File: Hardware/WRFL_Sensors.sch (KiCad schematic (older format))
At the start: 15 parts, among them P10 TEST_POINT, P11 TEST_POINT, P12 JST_XH_8, P9 TEST_POINT, U5 TPS73633DBV, U6 MS5611-01BA03

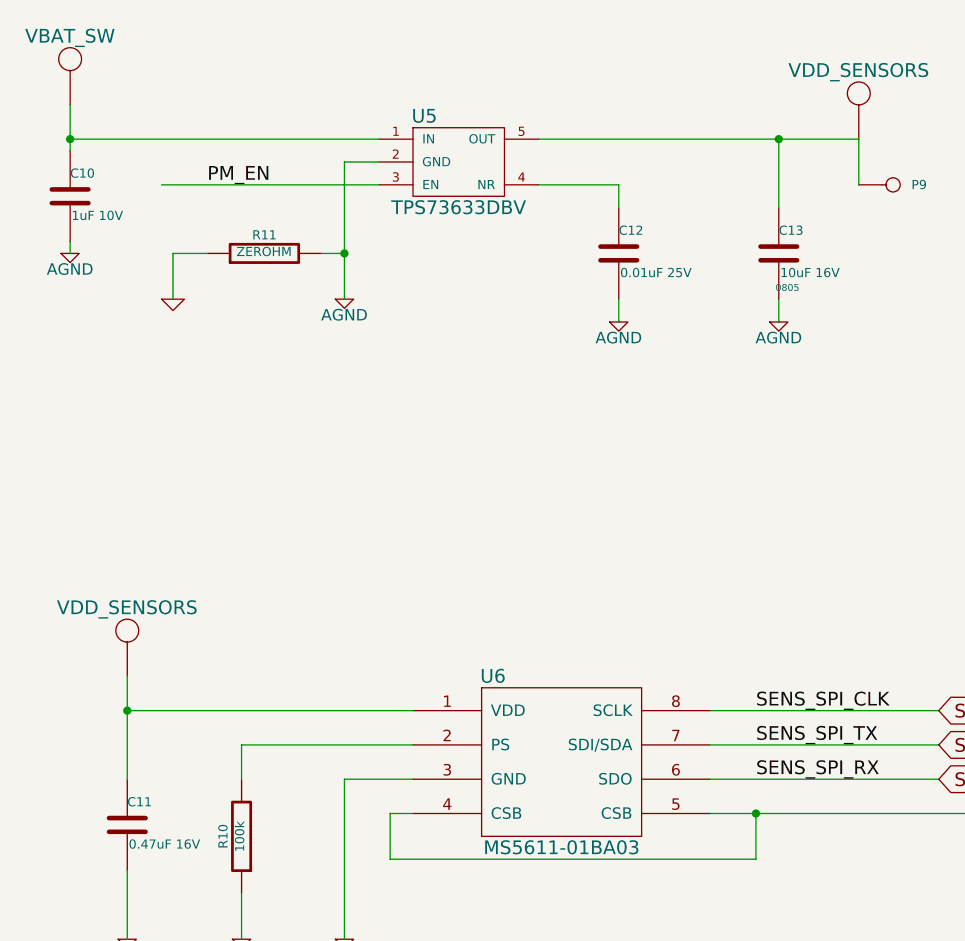
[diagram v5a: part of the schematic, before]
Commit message: MCU function assignment
BT RTS/CTS as test points,
BT reset GPIO option
Launchpad header pin function assignment (for ERC check)
Power symbols corrections
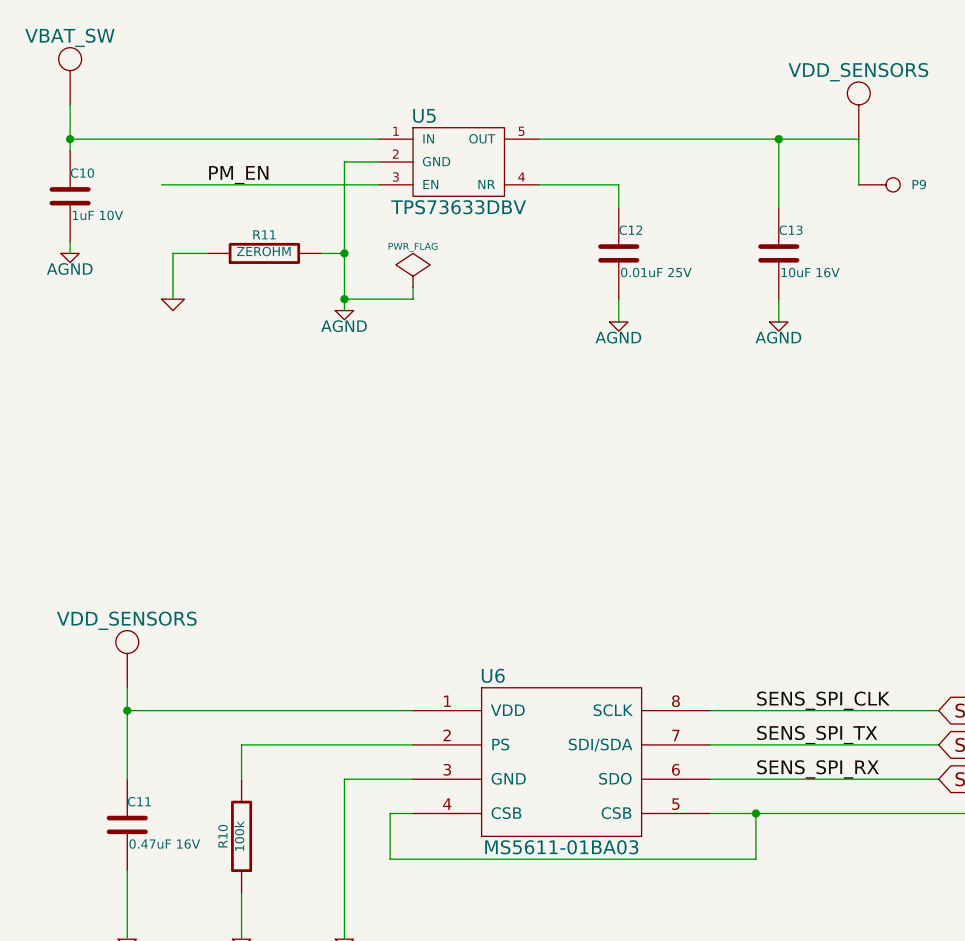
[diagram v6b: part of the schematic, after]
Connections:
- wire segments 50 -> 52
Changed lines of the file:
@@
-EESchema Schematic File Version 2  date Tuesday, October 15, 2013 09:37:22 AM
+EESchema Schematic File Version 2  date Tuesday, October 22, 2013 02:02:38 PM
 LIBS:power
 LIBS:device
@@
 Sheet 5 6
 Title ""
-Date "15 oct 2013"
+Date "22 oct 2013"
 Rev ""
 Comp "Nightmechanic"
@@
 Comment4 ""
 $EndDescr
-$Comp
-L VDD_SENSORS #U20
-U 1 1 524D591B
-P 4450 1800
-F 0 "#U20" H 4450 2000 60  0001 C CNN
-F 1 "VDD_SENSORS" H 4450 1900 60  0000 C CNN
-F 2 "" H 4450 1800 60  0000 C CNN
-F 3 "" H 4450 1800 60  0000 C CNN
-	1    4450 1800
-	1    0    0    -1
-$EndComp
 Wire Wire Line
 	1000 2450 1000 2500
@@
 $EndComp
 Wire Wire Line
-	2200 2100 2200 2700
+	2200 2100 2200 2750
 Wire Wire Line
 	2350 2100 2200 2100
@@
 	4100 2700 4100 2800
 $Comp
-L GND #PWR44
+L GND #PWR066
 U 1 1 524D593E
 P 1450 2700
-F 0 "#PWR44" H 1450 2700 30  0001 C CNN
+F 0 "#PWR066" H 1450 2700 30  0001 C CNN
 F 1 "GND" H 1450 2630 30  0001 C CNN
 F 2 "" H 1450 2700 60  0000 C CNN
@@
 $EndComp
 $Comp
-L AGND #PWR46
+L AGND #PWR067
 U 1 1 524D5944
-P 2200 2700
-F 0 "#PWR46" H 2200 2700 40  0001 C CNN
-F 1 "AGND" H 2200 2630 50  0000 C CNN
-F 2 "" H 2200 2700 60  0000 C CNN
-F 3 "" H 2200 2700 60  0000 C CNN
-	1    2200 2700
-	1    0    0    -1
-$EndComp
-$Comp
-L AGND #PWR49
+P 2200 2750
+F 0 "#PWR067" H 2200 2750 40  0001 C CNN
+F 1 "AGND" H 2200 2680 50  0000 C CNN
+F 2 "" H 2200 2750 60  0000 C CNN
+F 3 "" H 2200 2750 60  0000 C CNN
+	1    2200 2750
+	1    0    0    -1
+$EndComp
+$Comp
+L AGND #PWR068
 U 1 1 524D594A
 P 4100 2800
-F 0 "#PWR49" H 4100 2800 40  0001 C CNN
+F 0 "#PWR068" H 4100 2800 40  0001 C CNN
 F 1 "AGND" H 4100 2730 50  0000 C CNN
 F 2 "" H 4100 2800 60  0000 C CNN
@@
 $EndComp
 $Comp
-L AGND #PWR48
+L AGND #PWR069
 U 1 1 524D5950
 P 3400 2800
-F 0 "#PWR48" H 3400 2800 40  0001 C CNN
+F 0 "#PWR069" H 3400 2800 40  0001 C CNN
 F 1 "AGND" H 3400 2730 50  0000 C CNN
 F 2 "" H 3400 2800 60  0000 C CNN
@@
 F 0 "C13" H 4100 2600 40  0000 L CNN
 F 1 "10uF 16V" H 4106 2415 40  0000 L CNN
-F 2 "0805" H 4138 2350 30  0000 C CNN
+F 2 "0805" H 4138 2350 30  0001 C CNN
 F 3 "~" H 4100 2500 60  0000 C CNN
 	1    4100 2500
@@
 PM_EN
 $Comp
-L VBAT_SW #U18
+L VBAT_SW #U070
 U 1 1 5251CA9A
 P 1000 1650
-F 0 "#U18" H 1000 1850 60  0001 C CNN
+F 0 "#U070" H 1000 1850 60  0001 C CNN
 F 1 "VBAT_SW" H 1000 1750 60  0000 C CNN
 F 2 "~" H 1000 1650 60  0000 C CNN
@@
 $EndComp
 Connection ~ 1000 2000
-$Comp
-L VDD_SENSORS #U22
-U 1 1 5251CABC
-P 9350 900
-F 0 "#U22" H 9350 1100 60  0001 C CNN
-F 1 "VDD_SENSORS" H 9350 1000 60  0000 C CNN
-F 2 "~" H 9350 900 60  0000 C CNN
-F 3 "~" H 9350 900 60  0000 C CNN
-	1    9350 900
-	1    0    0    -1
-$EndComp
 $Comp
 L CONN_8 P12
@@
 $EndComp
 $Comp
-L AGND #PWR45
+L AGND #PWR071
 U 1 1 5251D2F7
 P 1750 5500
-F 0 "#PWR45" H 1750 5500 40  0001 C CNN
+F 0 "#PWR071" H 1750 5500 40  0001 C CNN
 F 1 "AGND" H 1750 5430 50  0000 C CNN
 F 2 "" H 1750 5500 60  0000 C CNN
@@
 $EndComp
 $Comp
-L VDD_SENSORS #U19
-U 1 1 5251D30C
-P 1250 4150
-F 0 "#U19" H 1250 4350 60  0001 C CNN
-F 1 "VDD_SENSORS" H 1250 4250 60  0000 C CNN
-F 2 "~" H 1250 4150 60  0000 C CNN
-F 3 "~" H 1250 4150 60  0000 C CNN
-	1    1250 4150
-	1    0    0    -1
-$EndComp
-$Comp
-L AGND #PWR47
+L AGND #PWR072
 U 1 1 5251D323
 P 2200 5500
-F 0 "#PWR47" H 2200 5500 40  0001 C CNN
+F 0 "#PWR072" H 2200 5500 40  0001 C CNN
 F 1 "AGND" H 2200 5430 50  0000 C CNN
 F 2 "" H 2200 5500 60  0000 C CNN
@@
 Wire Wire Line
 	2500 4500 1250 4500
-Wire Wire Line
-	1250 4350 1250 4800
 Wire Wire Line
 	1750 4650 1750 4800
@@
 Connection ~ 1250 4500
 $Comp
-L AGND #PWR43
+L AGND #PWR073
 U 1 1 5251D411
 P 1250 5500
-F 0 "#PWR43" H 1250 5500 40  0001 C CNN
+F 0 "#PWR073" H 1250 5500 40  0001 C CNN
 F 1 "AGND" H 1250 5430 50  0000 C CNN
 F 2 "" H 1250 5500 60  0000 C CNN
@@
 SENS_SPI_RX
 $Comp
-L AGND #PWR50
+L AGND #PWR074
 U 1 1 5251D4FC
 P 9900 1900
-F 0 "#PWR50" H 9900 1900 40  0001 C CNN
+F 0 "#PWR074" H 9900 1900 40  0001 C CNN
 F 1 "AGND" H 9900 1830 50  0000 C CNN
 F 2 "" H 9900 1900 60  0000 C CNN
@@
 	-1   0    0    1
 $EndComp
-$Comp
-L VDD_SENSORS #U21
-U 1 1 5251D9FD
+Wire Wire Line
+	5900 4000 5900 4250
+Wire Wire Line
+	5900 4750 5900 4950
+Connection ~ 5900 4950
+$Comp
+L AGND #PWR075
+U 1 1 5251DA81
+P 1000 2500
+F 0 "#PWR075" H 1000 2500 40  0001 C CNN
+F 1 "AGND" H 1000 2430 50  0000 C CNN
+F 2 "" H 1000 2500 60  0000 C CNN
+F 3 "" H 1000 2500 60  0000 C CNN
+	1    1000 2500
+	1    0    0    -1
+$EndComp
+Wire Wire Line
+	9900 1200 9900 1250
+Wire Wire Line
+	10100 1800 9900 1800
+Connection ~ 9900 1800
+$Comp
+L VDD_SENSORS #PWR076
+U 1 1 526652F5
+P 9350 900
+F 0 "#PWR076" H 9350 1100 60  0001 C CNN
+F 1 "VDD_SENSORS" H 9350 1000 60  0000 C CNN
+F 2 "~" H 9350 900 60  0000 C CNN
+F 3 "~" H 9350 900 60  0000 C CNN
+	1    9350 900
+	1    0    0    -1
+$EndComp
+$Comp
+L VDD_SENSORS #PWR077
+U 1 1 526653D2
 P 5900 3800
-F 0 "#U21" H 5900 4000 60  0001 C CNN
+F 0 "#PWR077" H 5900 4000 60  0001 C CNN
 F 1 "VDD_SENSORS" H 5900 3900 60  0000 C CNN
 F 2 "~" H 5900 3800 60  0000 C CNN
@@
 	1    0    0    -1
 $EndComp
-Wire Wire Line
-	5900 4000 5900 4250
-Wire Wire Line
-	5900 4750 5900 4950
-Connection ~ 5900 4950
-$Comp
-L AGND #PWR42
-U 1 1 5251DA81
-P 1000 2500
-F 0 "#PWR42" H 1000 2500 40  0001 C CNN
-F 1 "AGND" H 1000 2430 50  0000 C CNN
-F 2 "" H 1000 2500 60  0000 C CNN
-F 3 "" H 1000 2500 60  0000 C CNN
-	1    1000 2500
-	1    0    0    -1
-$EndComp
-Wire Wire Line
-	9900 1200 9900 1250
-Wire Wire Line
-	10100 1800 9900 1800
-Connection ~ 9900 1800
+$Comp
+L VDD_SENSORS #PWR078
+U 1 1 526653E1
+P 4450 1800
+F 0 "#PWR078" H 4450 2000 60  0001 C CNN
+F 1 "VDD_SENSORS" H 4450 1900 60  0000 C CNN
+F 2 "~" H 4450 1800 60  0000 C CNN
+F 3 "~" H 4450 1800 60  0000 C CNN
+	1    4450 1800
+	1    0    0    -1
+$EndComp
+$Comp
+L VDD_SENSORS #PWR079
+U 1 1 526653F0
+P 1250 4200
+F 0 "#PWR079" H 1250 4400 60  0001 C CNN
+F 1 "VDD_SENSORS" H 1250 4300 60  0000 C CNN
+F 2 "~" H 1250 4200 60  0000 C CNN
+F 3 "~" H 1250 4200 60  0000 C CNN
+	1    1250 4200
+	1    0    0    -1
+$EndComp
+Wire Wire Line
+	1250 4400 1250 4800
+$Comp
+L PWR_FLAG #FLG080
+U 1 1 52665DF6
+P 2500 2650
+F 0 "#FLG080" H 2500 2745 30  0001 C CNN
+F 1 "PWR_FLAG" H 2500 2830 30  0000 C CNN
+F 2 "" H 2500 2650 60  0000 C CNN
+F 3 "" H 2500 2650 60  0000 C CNN
+	1    2500 2650
+	1    0    0    -1
+$EndComp
+Wire Wire Line
+	2500 2650 2500 2700
+Wire Wire Line
+	2500 2700 2200 2700
+Connection ~ 2200 2700
 $EndSCHEMATC
